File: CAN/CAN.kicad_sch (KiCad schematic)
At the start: 23 parts, among them CN1 1.0T-4PLTPZ, J1 Conn_01x04, J2 Screw_Terminal_01x02, P1 USB_C_Plug_USB2.0, Q1 BSS214NW, Q2 BSS214NW, U1 AP2112K-3.3, U2 SN65HVD230, U5 ESP32-C3-MINI-1

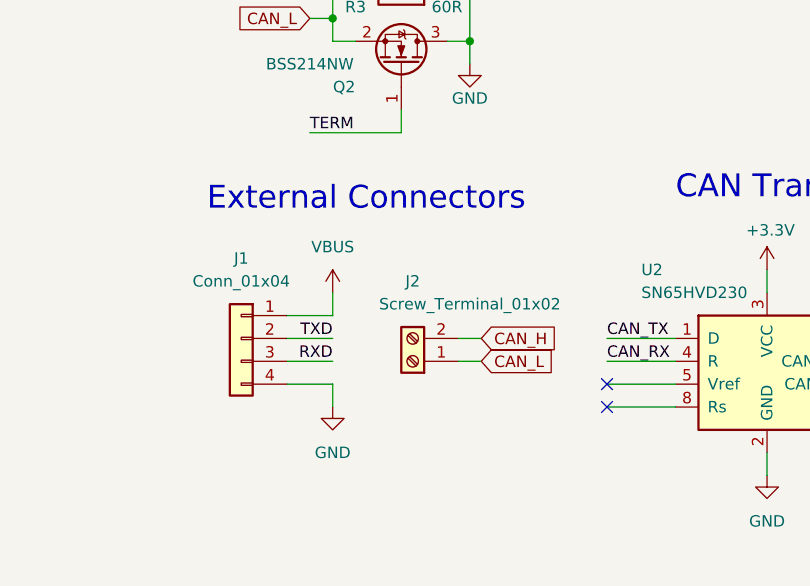
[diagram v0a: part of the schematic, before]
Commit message: Removed UART Pins
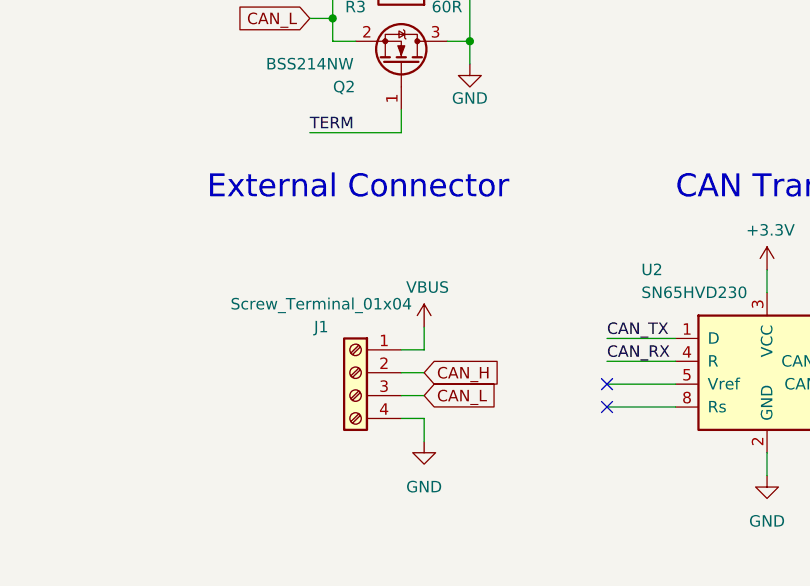
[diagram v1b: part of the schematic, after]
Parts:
- removed J1: Conn_01x04, Connector_PinSocket_2.54mm:PinSocket_1x04_P2.54mm_Horizontal, symbol Connector_Generic:Conn_01x04
- removed J2: Screw_Terminal_01x02, Connector_PinHeader_2.54mm:PinHeader_1x02_P2.54mm_Horizontal, symbol Connector:Screw_Terminal_01x02
- added J1: Screw_Terminal_01x04, symbol Connector:Screw_Terminal_01x04
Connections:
- net CAN_H: now also J1.2 (Pin_2)
- net CAN_L: now also J1.3 (Pin_3)
- net GND: now also J1.4 (Pin_4)
- net VBUS: now also J1.1 (Pin_1)
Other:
- note added: "External Connector"
- note removed: "External Connectors"

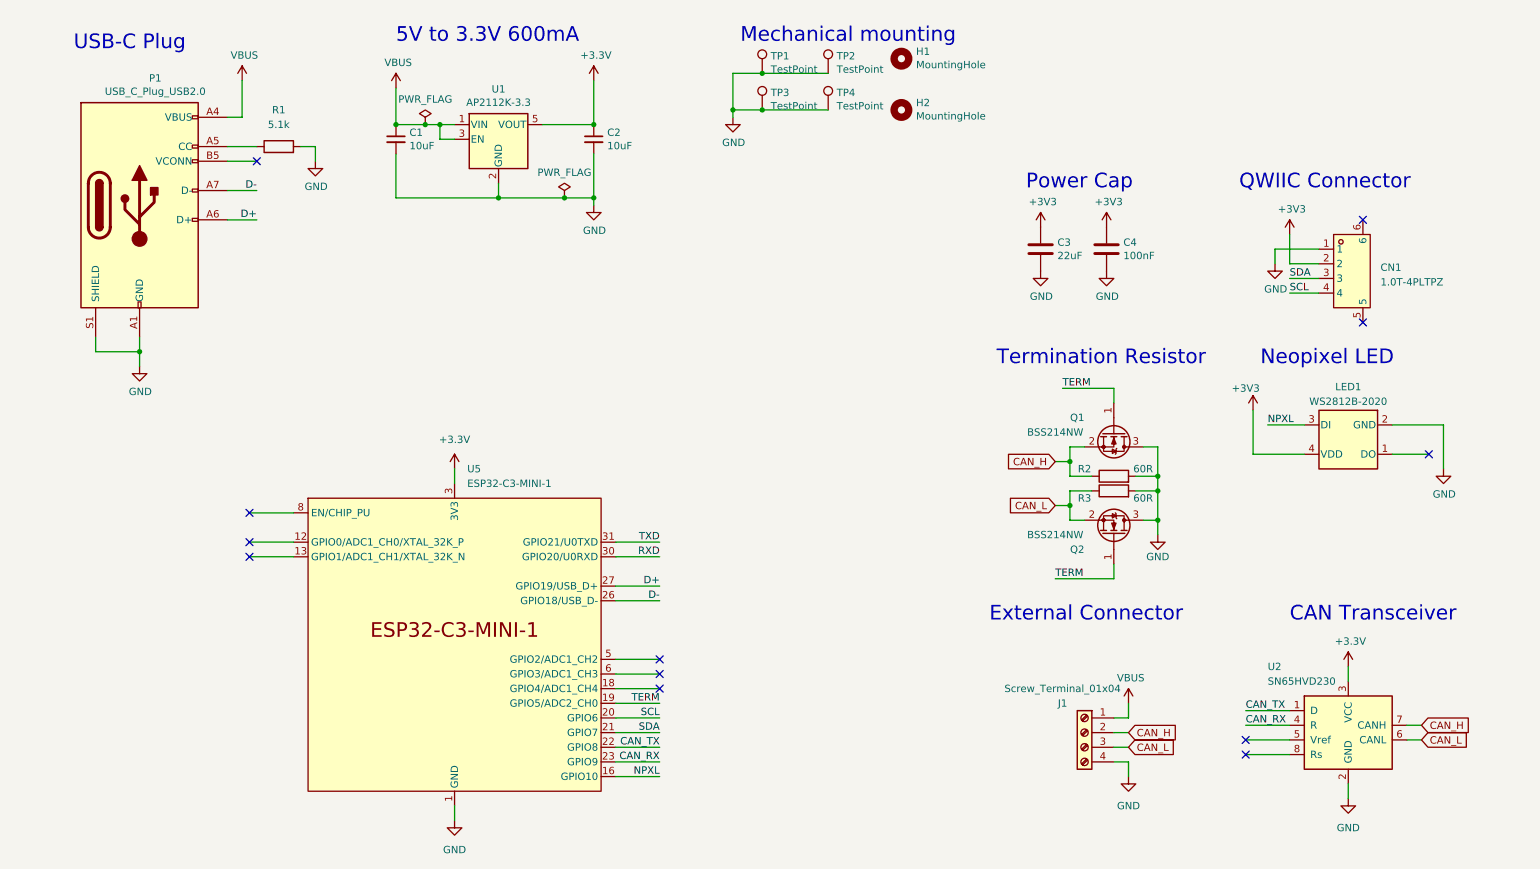
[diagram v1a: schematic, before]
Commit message: Added FSUB PDcontroller
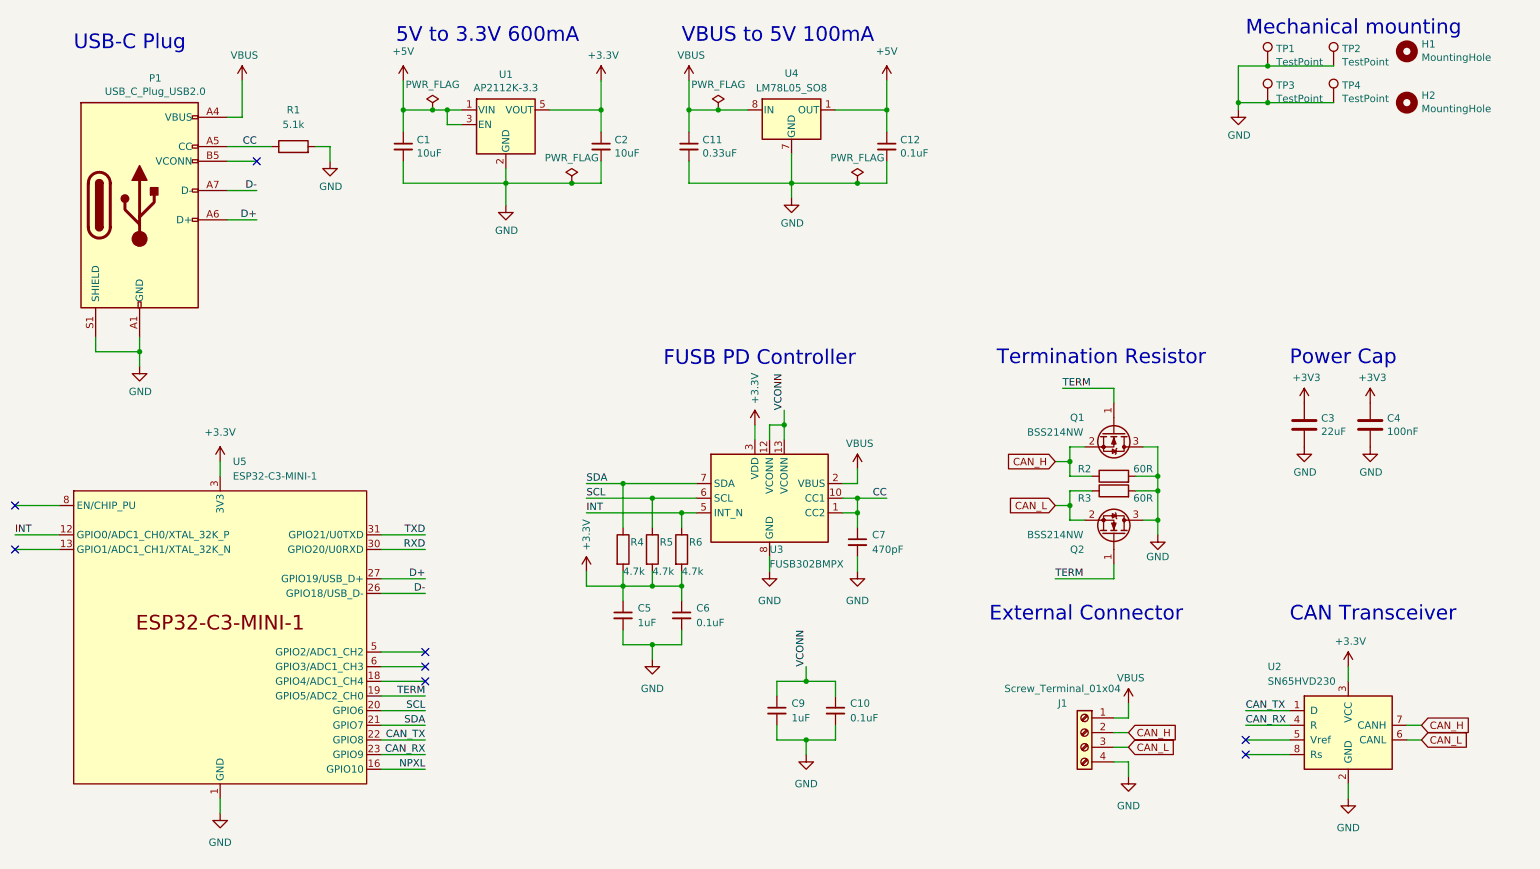
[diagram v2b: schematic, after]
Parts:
- removed CN1: 1.0T-4PLTPZ, _mykicadlib:FPC-SMD_4P-P1.00_1.0T-4PLTPZ, symbol _mykicadlib:QWIIC_1.0T-4PLTPZ
- removed LED1: WS2812B-2020, _mykicadlib:LED-SMD_4P-L2.0-W2.0-TL_WS2812B-2020, symbol _mykicadlib:WS2812B-2020
- added C10, C12, C6: 0.1uF, Capacitor_SMD:C_0201_0603Metric, symbol Device:C_Small
- added C11: 0.33uF, Capacitor_SMD:C_0201_0603Metric, symbol Device:C_Small
- added C5, C9: 1uF, Capacitor_SMD:C_0201_0603Metric, symbol Device:C_Small
- added C7: 470pF, Capacitor_SMD:C_0201_0603Metric, symbol Device:C_Small
- added R4, R5, R6: 4.7k, Resistor_SMD:R_0201_0603Metric, symbol Device:R
- added U3: FUSB302BMPX, Package_DFN_QFN:WQFN-14-1EP_2.5x2.5mm_P0.5mm_EP1.45x1.45mm, symbol Interface_USB:FUSB302BMPX
- added U4: LM78L05_SO8, Package_SO:SOIC-8_3.9x4.9mm_P1.27mm, symbol Regulator_Linear:LM78L05_SO8
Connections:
- net +3.3V: now also C5.1, C6.1, R4.2, R5.2, R6.2, U3.3 (VDD), U3.4 (VDD)
- net GND: now also C10.2, C11.2, C12.2, C5.2, C6.2, C7.2, C9.2, U3.15 (GND), U3.8 (GND), U3.9 (GND), U4.2 (GND), U4.3 (GND), U4.6 (GND), U4.7 (GND)
- net SCL: now also R5.1, U3.6 (SCL)
- net SDA: now also R4.1, U3.7 (SDA)
- net VBUS: now also C11.1, U3.2 (VBUS), U4.8 (IN); no longer C1.1, U1.1 (VIN), U1.3 (EN)
- net CC: now reaches P1.A5 (CC), R1.1
- net CC: now also C7.1, U3.1 (CC2), U3.10 (CC1), U3.11 (CC1), U3.14 (CC2)
- net INT: now reaches U5.12 (GPIO0/ADC1_CH0/XTAL_32K_P)
- net INT: now also R6.1, U3.5 (INT_N)
- new net +5V: C1.1, C12.1, U1.1 (VIN), U1.3 (EN), U4.1 (OUT)
- new net VCONN: C10.1, C9.1, U3.12 (VCONN), U3.13 (VCONN)
- no-connect marks 12 -> 8
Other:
- note added: "FUSB PD Controller"
- note added: "VBUS to 5V 100mA"
- note removed: "Neopixel LED"
- note removed: "QWIIC Connector"
- moved on the sheet: C1, C2, C3, C4, H1, H2, R1, TP1, TP2, TP3, TP4, U1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
